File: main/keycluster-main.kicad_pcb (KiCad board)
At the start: 2 copper layers, 45.1 x 52.6 mm, 39 parts, among them P2 CONN_5, P7 CONN_10, P8 CONN_7, SW1 S01_Socket, SW2 S01_Socket, SW3 S01_Socket, SW4 CMI126603D08, SW6 CMI126603D08, U1 MKL17Z32VFM4, U4 ESD

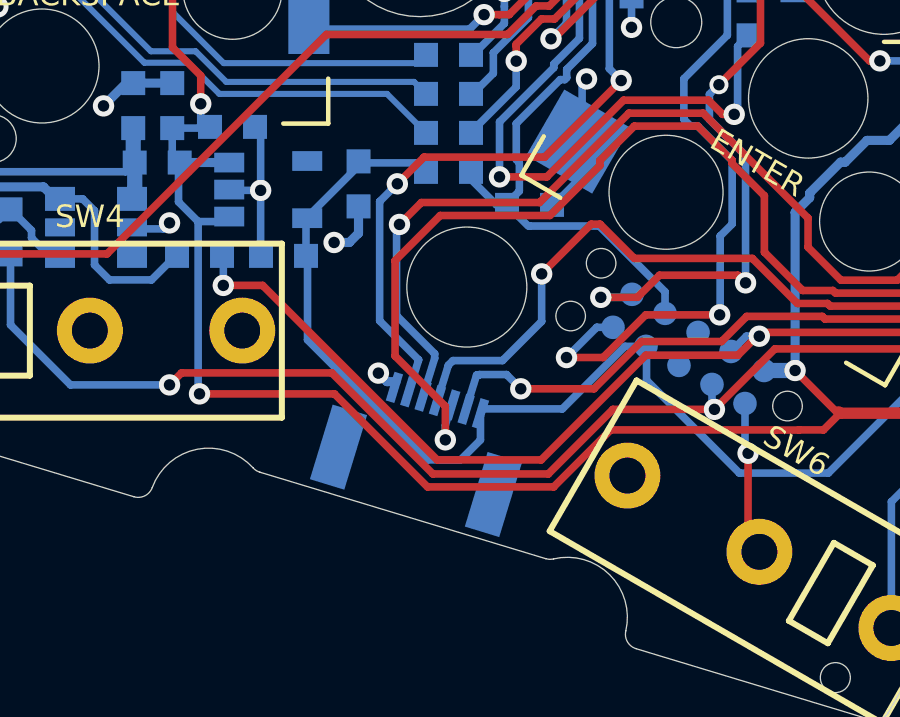
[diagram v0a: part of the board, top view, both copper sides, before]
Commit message: Move the FFC connector by about 0.8 mm away from the edge of the main board.
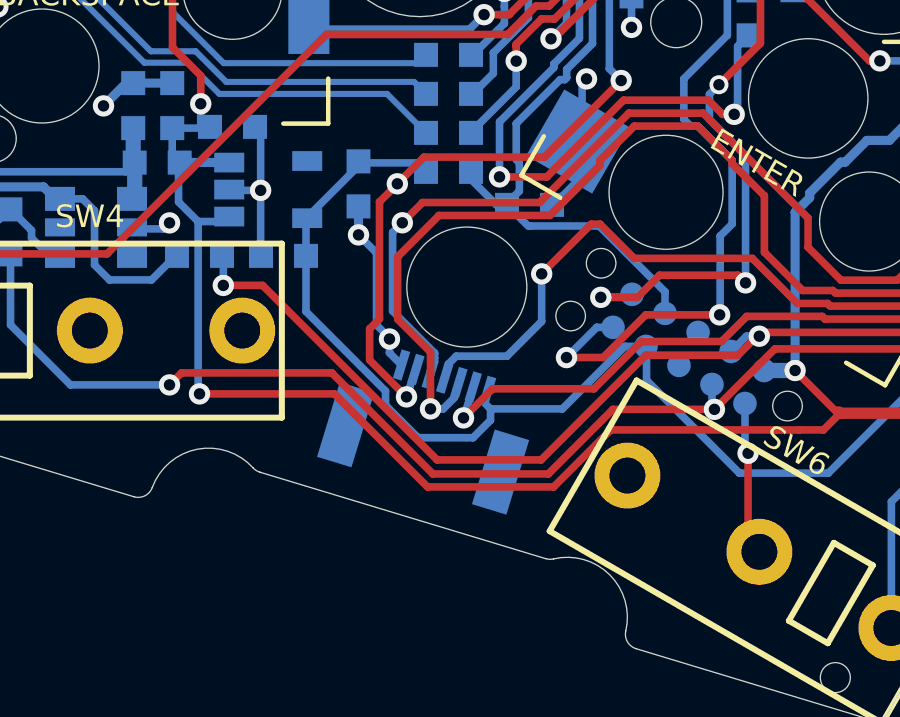
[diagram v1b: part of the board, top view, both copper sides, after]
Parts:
- moved P8 0.78 mm to (142.9, 126.0)
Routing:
- net GND: track 43.5 -> 46.7 mm
- net /SW5: track 25.6 -> 27.0 mm, vias 2 -> 3
- net /TB_DOWN: track 51.7 -> 50.5 mm
- net /TB_UP: track 42.9 -> 42.0 mm
- net /TB_LEFT: track 40.8 -> 41.6 mm
- net +3V3: track 67.6 -> 67.0 mm

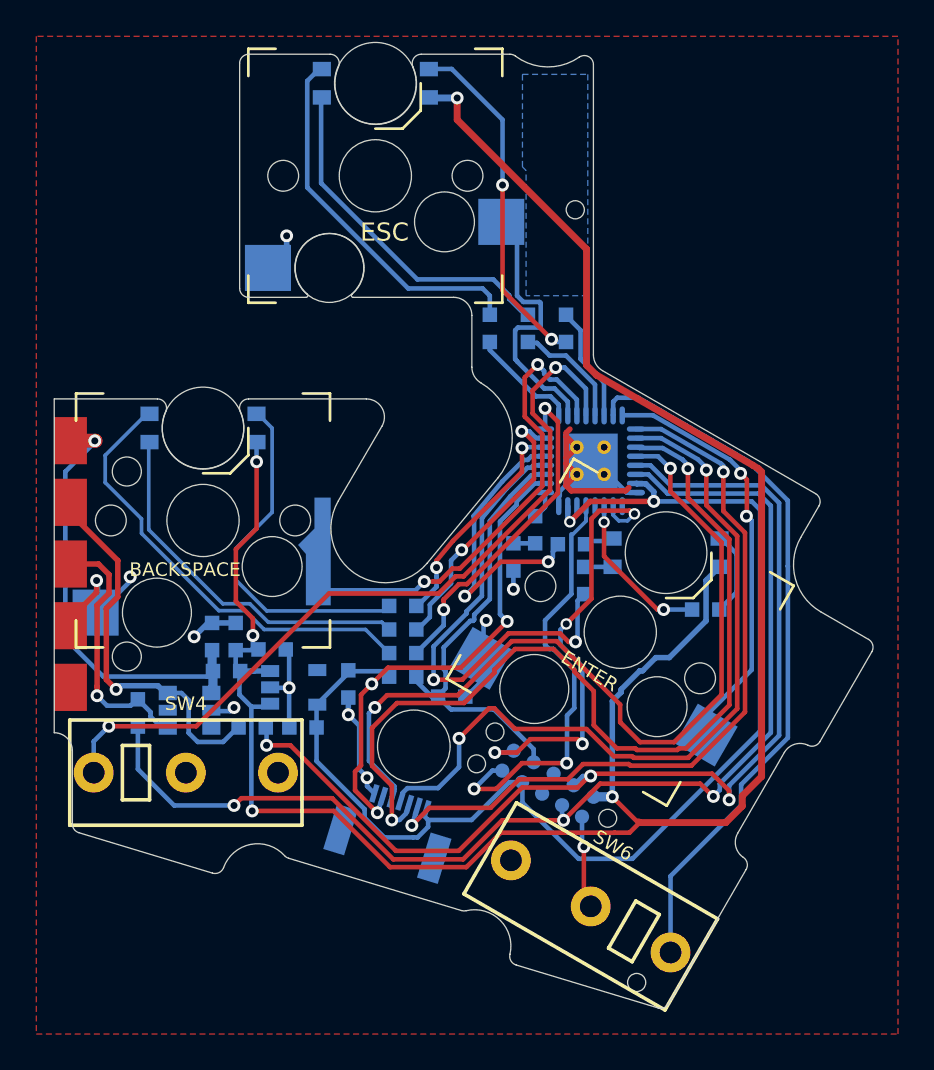
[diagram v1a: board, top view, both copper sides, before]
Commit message: Update board based on CAD.
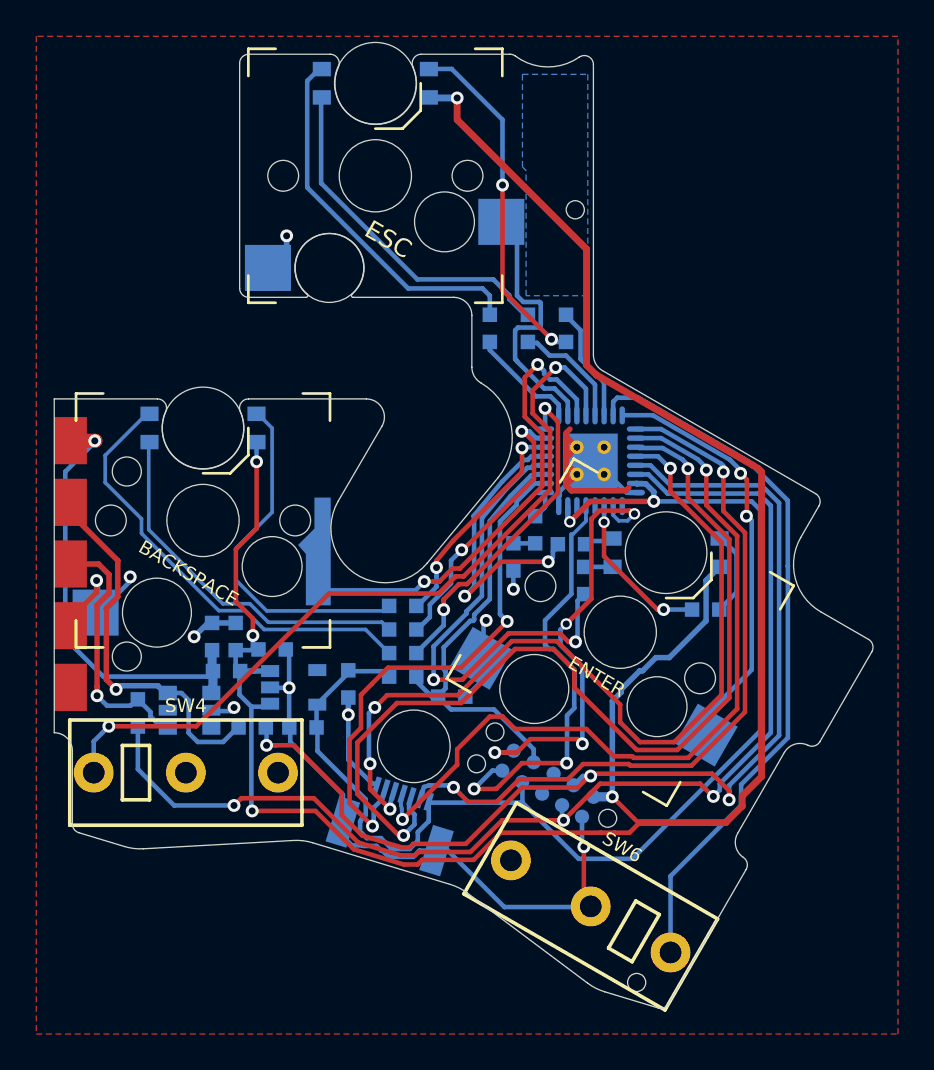
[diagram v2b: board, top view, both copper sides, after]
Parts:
- moved P8 0.44 mm to (143.0, 125.6)
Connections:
- P8 pad : (no net) -> GND
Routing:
- net GND: track 46.7 -> 68.1 mm, vias 11 -> 10
- net /SW5: track 27.0 -> 29.2 mm, vias 3 -> 2
- net /TB_DOWN: track 50.5 -> 52.1 mm
- net /TB_RIGHT: track 46.2 -> 47.7 mm, vias 2 -> 4
- net +3V3: track 67.0 -> 68.4 mm
- net /TB_LEFT: track 41.6 -> 40.4 mm
- net /TB_UP: track 42.0 -> 43.2 mm
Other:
- outline, holes or cut-outs redrawn

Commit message: Bump main board version to 2.4.0
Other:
- board text added: "PCB ID: keycluster_main_2.4.0"
- board text removed: "PCB ID: keycluster_main_2.3.0"
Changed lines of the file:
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@@
   (title_block
     (title "UHK Key Cluster Module - Main Board")
-    (rev 2.3.0)
+    (rev 2.4.0)
     (company "Ultimate Gadget Laboratories Kft.")
   )
@@
     )
   )
-  (gr_text "PCB ID:\nkeycluster_main_2.3.0" (at 162.493312 121.437542 60) (layer B.SilkS)
+  (gr_text "PCB ID:\nkeycluster_main_2.4.0" (at 162.493312 121.437542 60) (layer B.SilkS)
     (effects (font (size 0.75 0.75) (thickness 0.15)) (justify mirror))
   )

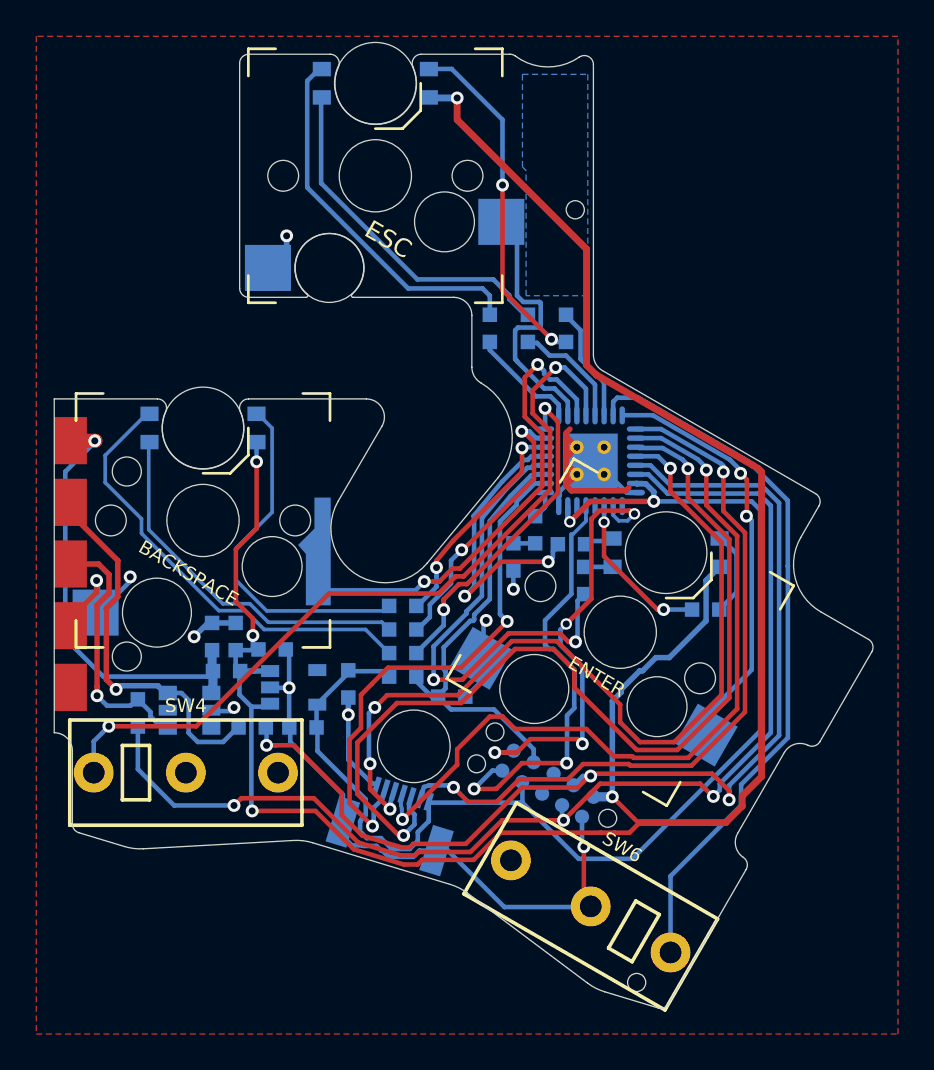
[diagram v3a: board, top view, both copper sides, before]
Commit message: Update PCB with new components.
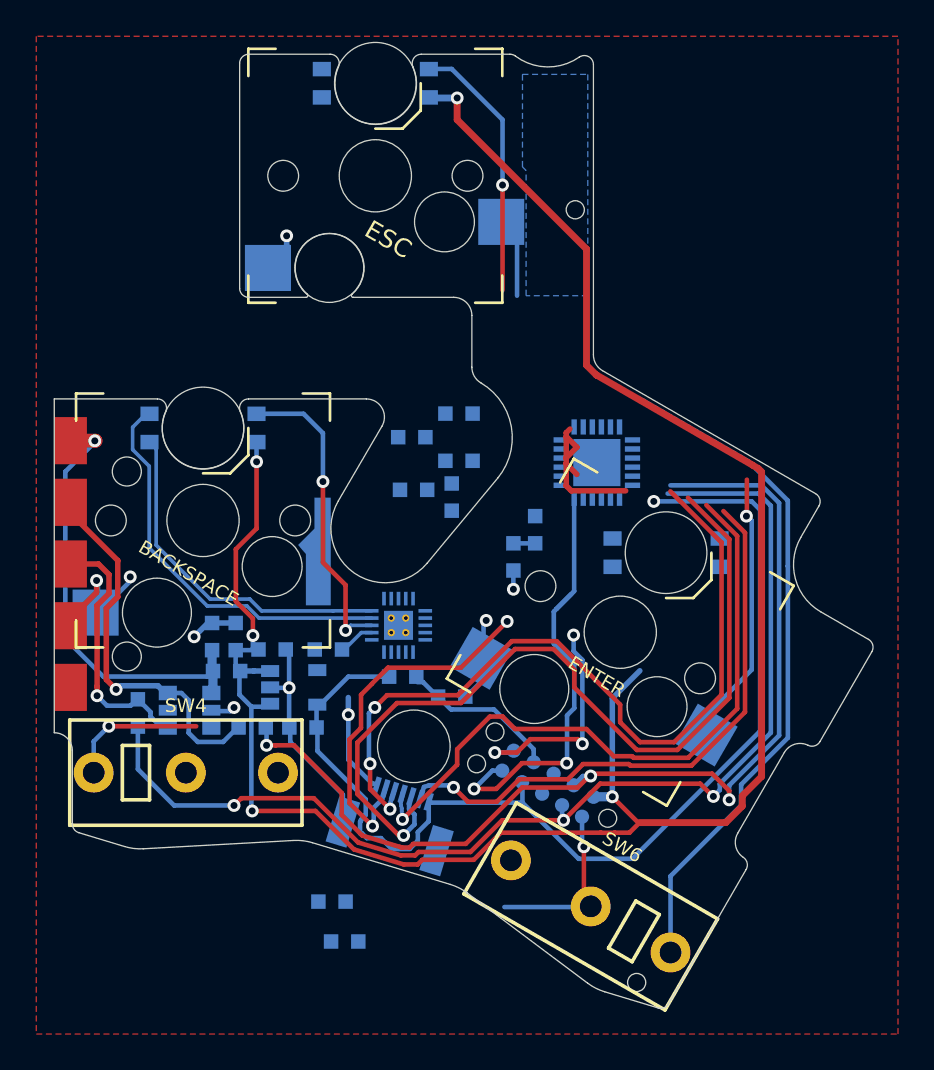
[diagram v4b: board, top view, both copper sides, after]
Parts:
- removed R10, R11, R12, R13, R8, R9: 330, UGL:SM0603
- added C1: 0.1uF, UGL:SM0603, B.Cu at (147.3, 103.4)
- added C5: 0.1uF, UGL:SM0603, B.Cu at (140.1, 113.8)
- added C6: 0.22uF, UGL:SM0603, B.Cu at (140.3, 127.7)
- added C9: 0.1uF, UGL:SM0603, B.Cu at (144.8, 105.0)
- added U2: IS31FL3199, UGL:QFN-20_EP_3x3_Pitch0.4mm, B.Cu at (144.0, 112.5)
- R3, R4: value 330 -> 100k
- R5: value 330 -> 10k
- U1: value MKL17Z32VFM4 -> MKL03Z32VFK4; footprint UGL:QFN-32_EP_5x5_Pitch0.5mm -> UGL:QFN-24-1EP_4x4mm_Pitch0.5mm
- moved R4 16.2 mm to (141.0, 129.9)
- moved R3 12.3 mm to (147.3, 100.8)
- moved C4 11.8 mm to (146.9, 105.4)
- moved R5 9.31 mm to (144.7, 102.1)
- moved U1 0.36 mm to (154.9, 103.5), turned to 0 degrees
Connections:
- P8 pad : GND -> (no net)
- R3 pad 1: Net-(D2-Pad2) -> GND
- R3 pad 2: /TPM0_CH1 -> /SDB
- R4 pad 1: Net-(D2-Pad1) -> GND
- R4 pad 2: /TPM0_CH2 -> Net-(R4-Pad2)
- R5 pad 1: Net-(D2-Pad3) -> Net-(R5-Pad1)
- R5 pad 2: /TPM0_CH0 -> /CLK
- U1 pad 1: /TB_LEFT -> /TB_RIGHT
- U1 pad 10: /SWDCLK -> /CLK
- U1 pad 11: /TPM2_CH0 -> Net-(U1-Pad11)
- U1 pad 12: Net-(U1-Pad12) -> /SDB
- U1 pad 13: /SWDIO -> /TEST_LED
- U1 pad 14: Net-(U1-Pad14) -> /SW3
- U1 pad 15: +3V3 -> /SW6
- U1 pad 16: GND -> Net-(U1-Pad16)
- U1 pad 17: /TEST_LED -> /SCL
- U1 pad 18: /SW5 -> /SDA
- U1 pad 19: /RESET -> Net-(U1-Pad19)
- U1 pad 2: /TB_UP -> /SW5
- U1 pad 20: /TPM1_CH0 -> Net-(U1-Pad20)
- U1 pad 21: /TPM1_CH1 -> /TB_LEFT
- U1 pad 22: /TPM0_CH0 -> /SWDCLK
- U1 pad 23: /TPM0_CH1 -> /RESET
- U1 pad 24: /TPM0_CH2 -> /SWDIO
- U1 pad 25: /TPM0_CH3 -> GND
- U1 pad 3: /TB_DOWN -> +3V3
- U1 pad 4: /TB_RIGHT -> GND
- U1 pad 5: /SDA -> /TB_UP
- U1 pad 6: /SCL -> /TB_DOWN
- U1 pad 7: +3V3 -> /SW4
- U1 pad 8: GND -> /SW2
- U1 pad 9: Net-(U1-Pad9) -> /SW1
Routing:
- net /SW4: track 43.9 -> 7.72 mm, vias 2 -> 1
- net /TPM1_CH0: track 26.7 -> 0.00 mm, vias 2 -> 0
- net /SW2: track 25.6 -> 0.00 mm, vias 2 -> 0
- net Net-(D1-Pad1): track 20.0 -> 0.00 mm
- net Net-(D1-Pad2): track 18.7 -> 0.00 mm
- net /TPM0_CH2: track 18.4 -> 0.00 mm, vias 2 -> 0
- net /TPM1_CH1: track 16.6 -> 0.00 mm, vias 2 -> 0
- net GND: track 68.1 -> 51.5 mm
- net /TPM0_CH1: track 15.4 -> 0.00 mm, vias 2 -> 0
- net /RESET: track 23.8 -> 8.68 mm
- net /TPM0_CH0: track 12.4 -> 0.00 mm, vias 2 -> 0
- net /SWDCLK: track 24.5 -> 12.5 mm, vias 4 -> 3
- net /SW1: track 14.8 -> 4.33 mm
- net /SW5: track 29.2 -> 20.0 mm
- net /TPM2_CH0: track 8.83 -> 0.00 mm, vias 2 -> 0
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
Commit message: Routing.
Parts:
- removed C9: 0.1uF, UGL:SM0603
- removed G***: LOGO, UGL:UHK_Logo_12x3.4_mm
- removed hole (x2): 1.0mm, UGL:hole_1.0mm
- moved R4 15.4 mm to (145.7, 115.2), turned to 90 degrees
- moved C1 13.8 mm to (141.0, 115.7), turned to 90 degrees
- moved D7 13.3 mm to (157.1, 97.3)
- moved C6 12.4 mm to (145.1, 116.3), turned to 0 degrees
- moved R2 12.1 mm to (158.6, 97.4)
- moved C3 10.2 mm to (152.1, 107.6), turned to 90 degrees
- moved R1 10.1 mm to (150.8, 107.6), turned to 90 degrees
- moved C4 4.91 mm to (151.0, 102.8), turned to 270 degrees
- moved U2 0.33 mm to (144.0, 112.8)
- moved D3 0.09 mm to (158.8, 108.5)
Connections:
- U1 pad 16: Net-(U1-Pad16) -> /TB_LEFT
- U1 pad 21: /TB_LEFT -> /TB_UP
- U1 pad 5: /TB_UP -> /TB_DOWN
- U1 pad 6: /TB_DOWN -> Net-(U1-Pad6)
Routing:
- net /TB_DOWN: track 47.1 -> 2.10 mm
- net Net-(D1-Pad1): track 0.00 -> 41.5 mm, vias 0 -> 2
- net Net-(D1-Pad2): track 0.00 -> 37.7 mm, vias 0 -> 2
- net /SW2: track 0.00 -> 29.0 mm, vias 0 -> 2
- net Net-(D3-Pad3): track 0.40 -> 29.2 mm, vias 0 -> 2
- net Net-(D1-Pad3): track 14.6 -> 37.4 mm, vias 1 -> 2
- net /TB_RIGHT: track 44.2 -> 24.3 mm, vias 3 -> 2
- net GND: track 51.5 -> 32.3 mm, vias 10 -> 9
- net Net-(D3-Pad1): track 0.20 -> 15.3 mm, vias 0 -> 2
- net /SCL: track 62.4 -> 76.5 mm, vias 3 -> 4
- net +3V3: track 60.7 -> 47.1 mm, vias 1 -> 2
- net /RESET: track 8.68 -> 21.6 mm, vias 0 -> 2
- net Net-(D3-Pad2): track 0.01 -> 12.4 mm, vias 0 -> 2
- net /TB_UP: track 36.7 -> 25.7 mm, vias 1 -> 2
- net /SWDCLK: track 12.5 -> 21.8 mm, vias 3 -> 2
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- removed copper zone on B.Cu, net (none)

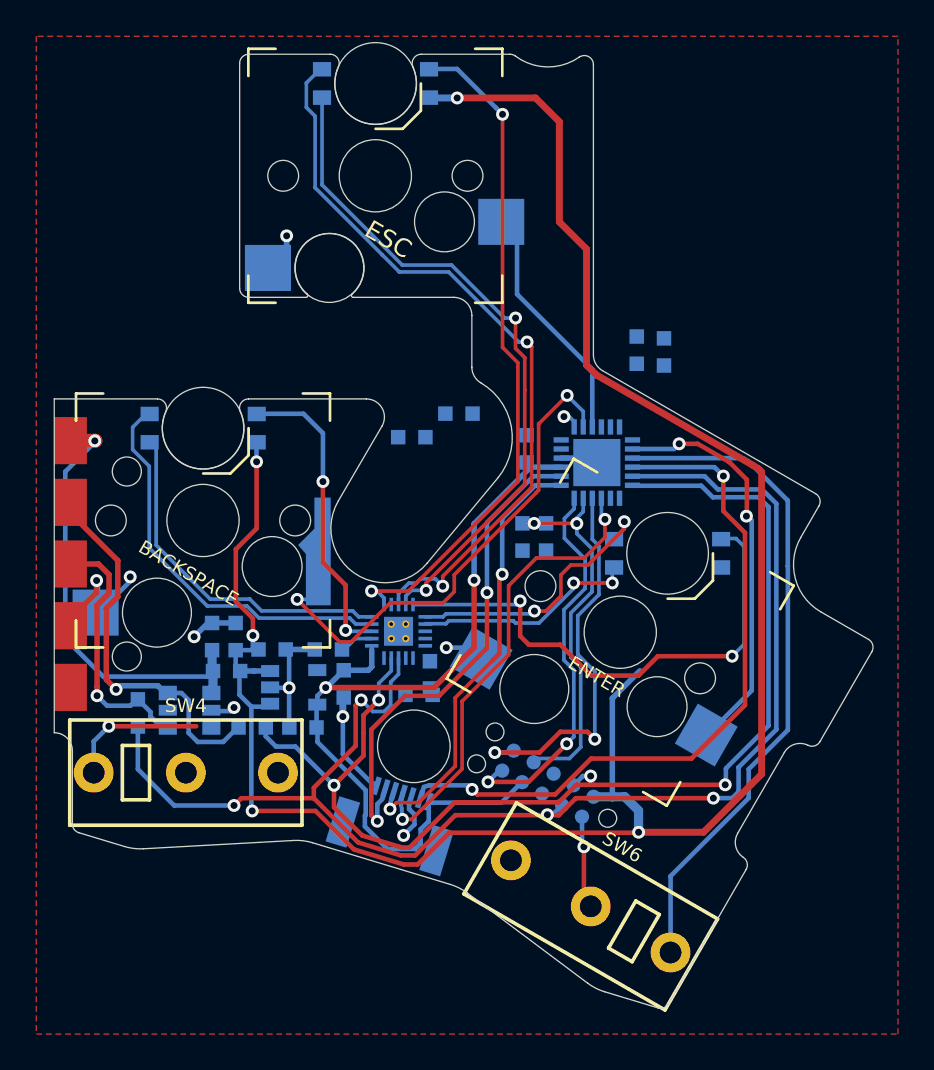
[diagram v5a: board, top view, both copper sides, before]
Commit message: Reallocate control pins on schematic and routing on PCB.
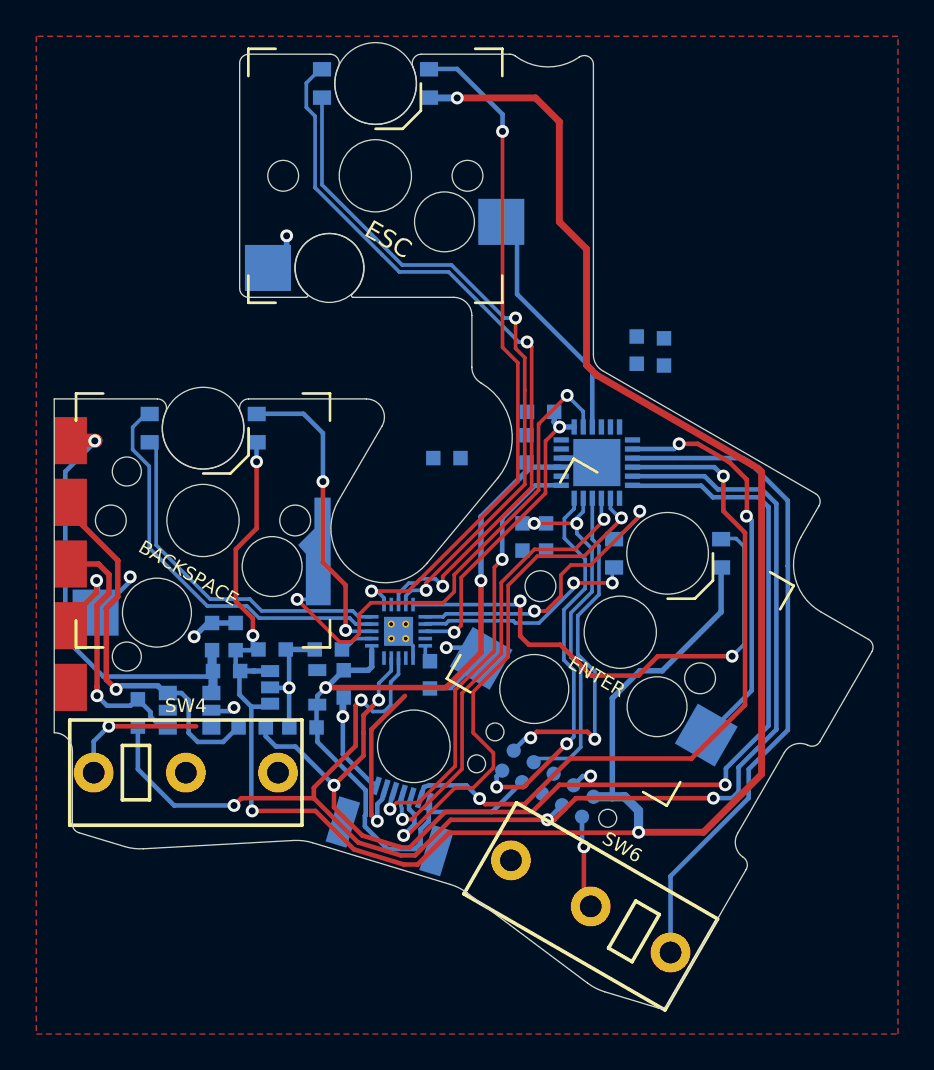
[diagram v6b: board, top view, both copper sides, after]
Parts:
- removed C6: 0.22uF, UGL:SM0603
- moved R3 4.50 mm to (151.8, 100.7)
- moved R5 2.25 mm to (146.6, 103.3)
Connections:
- U1 pad 11: Net-(U1-Pad11) -> /TEST_LED
- U1 pad 12: /SDB -> /SW4
- U1 pad 13: /TEST_LED -> /SW5
- U1 pad 2: /SW5 -> Net-(U1-Pad2)
- U1 pad 20: Net-(U1-Pad20) -> /TB_DOWN
- U1 pad 5: /TB_DOWN -> Net-(U1-Pad5)
- U1 pad 7: /SW4 -> /SDB
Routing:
- net /TB_DOWN: track 2.10 -> 29.1 mm, vias 1 -> 2
- net /SW5: track 27.4 -> 9.75 mm, vias 2 -> 1
- net /SDB: track 0.00 -> 17.4 mm, vias 0 -> 2
- net +5V: track 117.6 -> 125.9 mm
- net GND: track 32.3 -> 37.0 mm
- net /SWDCLK: track 21.8 -> 19.6 mm
- net Net-(D3-Pad1): track 15.3 -> 17.3 mm
- net +3V3: track 47.1 -> 48.2 mm
- net /SW4: track 8.69 -> 7.72 mm, vias 2 -> 1
- net Net-(R4-Pad2): track 0.00 -> 0.96 mm
- net /SW2: track 29.0 -> 29.6 mm

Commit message: Routing.
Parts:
- moved R5 12.3 mm to (158.7, 105.5), turned to 180 degrees
- moved R2 4.74 mm to (153.9, 96.8), turned to 270 degrees
- moved D7 4.53 mm to (152.6, 96.8)
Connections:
- U1 pad 10: /CLK -> /TEST_LED
- U1 pad 11: /TEST_LED -> Net-(U1-Pad11)
- U1 pad 12: /SW4 -> Net-(U1-Pad12)
- U1 pad 13: /SW5 -> /SW4
- U1 pad 19: Net-(U1-Pad19) -> /CLK
- U1 pad 2: Net-(U1-Pad2) -> /SW5
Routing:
- net /SW4: track 7.72 -> 44.3 mm, vias 1 -> 2
- net /SW5: track 9.75 -> 27.6 mm, vias 1 -> 2
- net Net-(R5-Pad1): track 0.00 -> 12.4 mm, vias 0 -> 1
- net Net-(D3-Pad3): track 29.2 -> 23.2 mm, vias 2 -> 1
- net /TEST_LED: track 0.00 -> 4.51 mm
- net GND: track 37.0 -> 41.4 mm, vias 9 -> 13
- net +3V3: track 48.2 -> 52.2 mm
- net Net-(D3-Pad1): track 17.3 -> 13.8 mm
- net /CLK: track 0.00 -> 1.81 mm
- net /TEST_LED_R: track 0.00 -> 1.30 mm
- net /SWDIO: track 21.0 -> 20.0 mm
- net /SW1: track 13.3 -> 14.1 mm
- net /SWDCLK: track 19.6 -> 18.8 mm
- net Net-(D3-Pad2): track 12.4 -> 13.1 mm
